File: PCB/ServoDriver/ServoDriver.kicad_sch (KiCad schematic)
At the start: 4 parts, among them Q1 IRF6775M, Q2 IRF6775M, Q3 IRF6775M, Q4 IRF6775M

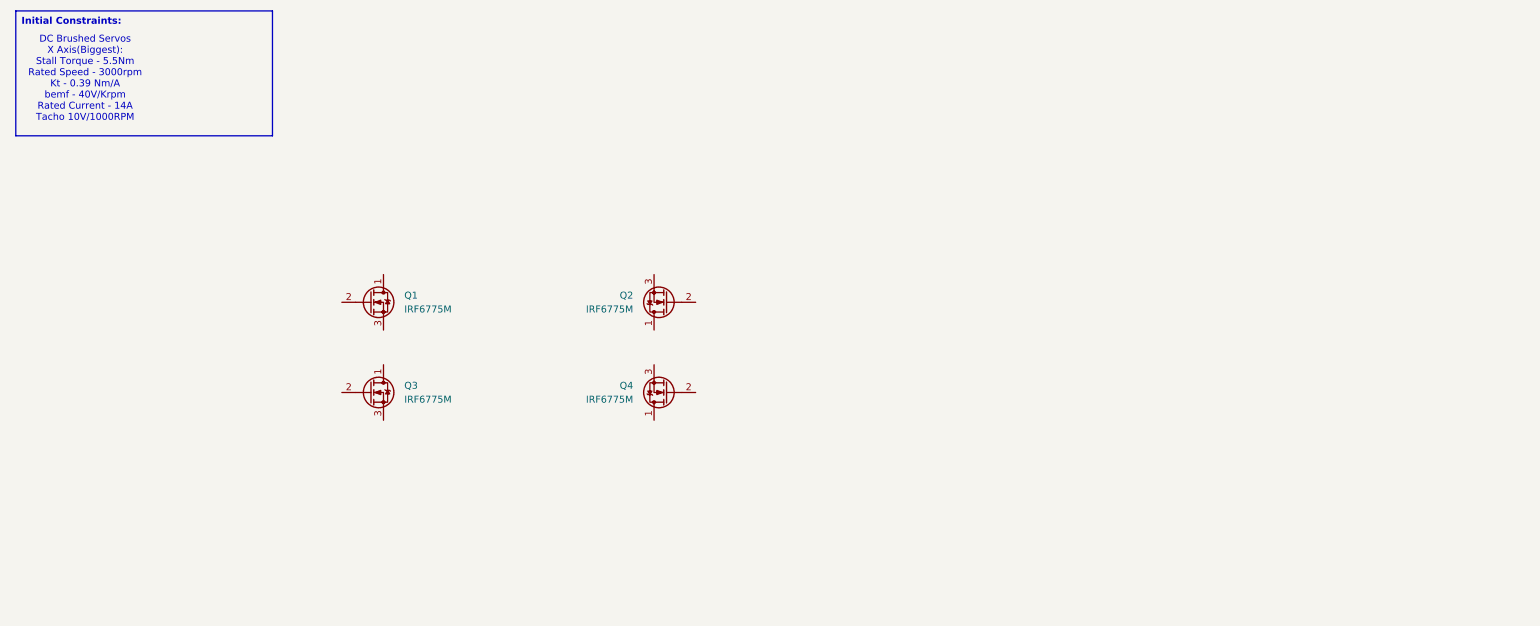
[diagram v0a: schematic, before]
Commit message: H-Bridge & Component Selection
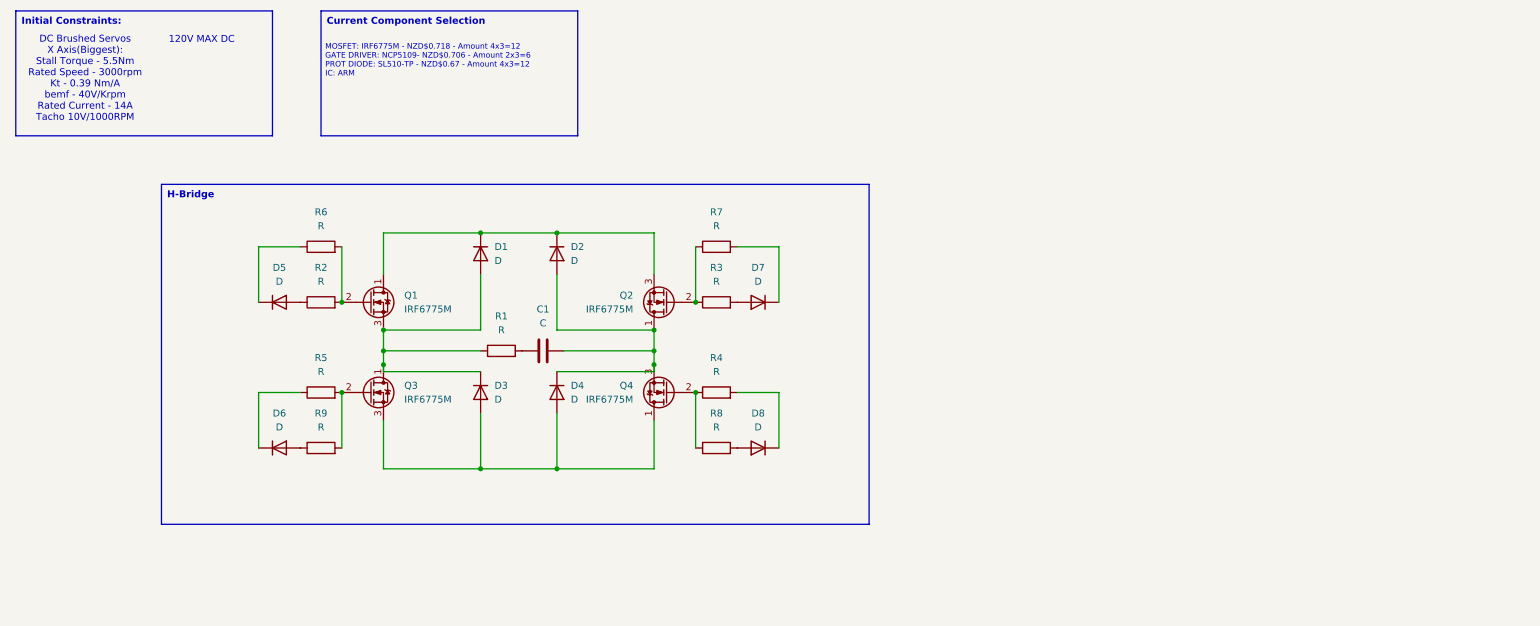
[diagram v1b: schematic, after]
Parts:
- added C1: C, symbol Device:C
- added D1, D2, D3, D4, D5, D6, D7, D8: D, symbol Device:D
- added R1, R2, R3, R4, R5, R6, R7, R8, R9: R, symbol Device:R
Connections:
- net at Q1.1 (D): now also Q2.3 (S), D1.1 (K), D2.1 (K)
- net at Q1.2 (G): now also R2.2, R6.2
- net at Q1.3 (S): now also Q3.1 (D), D1.2 (A), D3.1 (K), R1.1
- net at Q4.1 (D): now also Q3.3 (S), D3.2 (A), D4.2 (A)
- net at Q4.2 (G): now also R4.1, R8.1
- net at Q4.3 (S): now also Q2.1 (D), C1.2, D2.2 (A), D4.1 (K)
- net at Q2.2 (G): now also R3.1, R7.1
- net at Q3.2 (G): now also R5.2, R9.2
- new net: D5.1 (K), R6.1
- new net: D5.2 (A), R2.1
- new net: D8.1 (K), R4.2
- new net: D8.2 (A), R8.2
- new net: D7.2 (A), R3.2
- new net: D6.1 (K), R5.1
- new net: D6.2 (A), R9.1
- new net: D7.1 (K), R7.2
- new net: C1.1, R1.2
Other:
- note added: "120V MAX DC"
- note added: "MOSFET: IRF6775M - NZD$0.718 - Amount 4x3=12 GATE DRIVER: NCP5109- NZD$0.706 - Amount 2x3=6 PROT DIODE: SL510-TP - NZD$0.67 - Amount 4x3=12 IC: ARM"

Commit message: Fusion 360 Archive file
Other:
- note added: "MOSFET: IRF6775M - NZD$0.718 - Amount 4x3=12 GATE DRIVER: NCP5109- NZD$0.706 - Amount 2x3=6 PROT DIODE: SL510-TP - NZD$0.67 - Amount 4x3=12 IC: STM32F031x4"
- note removed: "MOSFET: IRF6775M - NZD$0.718 - Amount 4x3=12 GATE DRIVER: NCP5109- NZD$0.706 - Amount 2x3=6 PROT DIODE: SL510-TP - NZD$0.67 - Amount 4x3=12 IC: ARM"
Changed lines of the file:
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@@
 		)
 	)
-	(text "MOSFET: IRF6775M - NZD$0.718 - Amount 4x3=12\nGATE DRIVER: NCP5109- NZD$0.706 - Amount 2x3=6\nPROT DIODE: SL510-TP - NZD$0.67 - Amount 4x3=12\nIC: ARM\n"
+	(text "MOSFET: IRF6775M - NZD$0.718 - Amount 4x3=12\nGATE DRIVER: NCP5109- NZD$0.706 - Amount 2x3=6\nPROT DIODE: SL510-TP - NZD$0.67 - Amount 4x3=12\nIC: STM32F031x4\n"
 		(exclude_from_sim no)
 		(at 71.882 24.384 0)

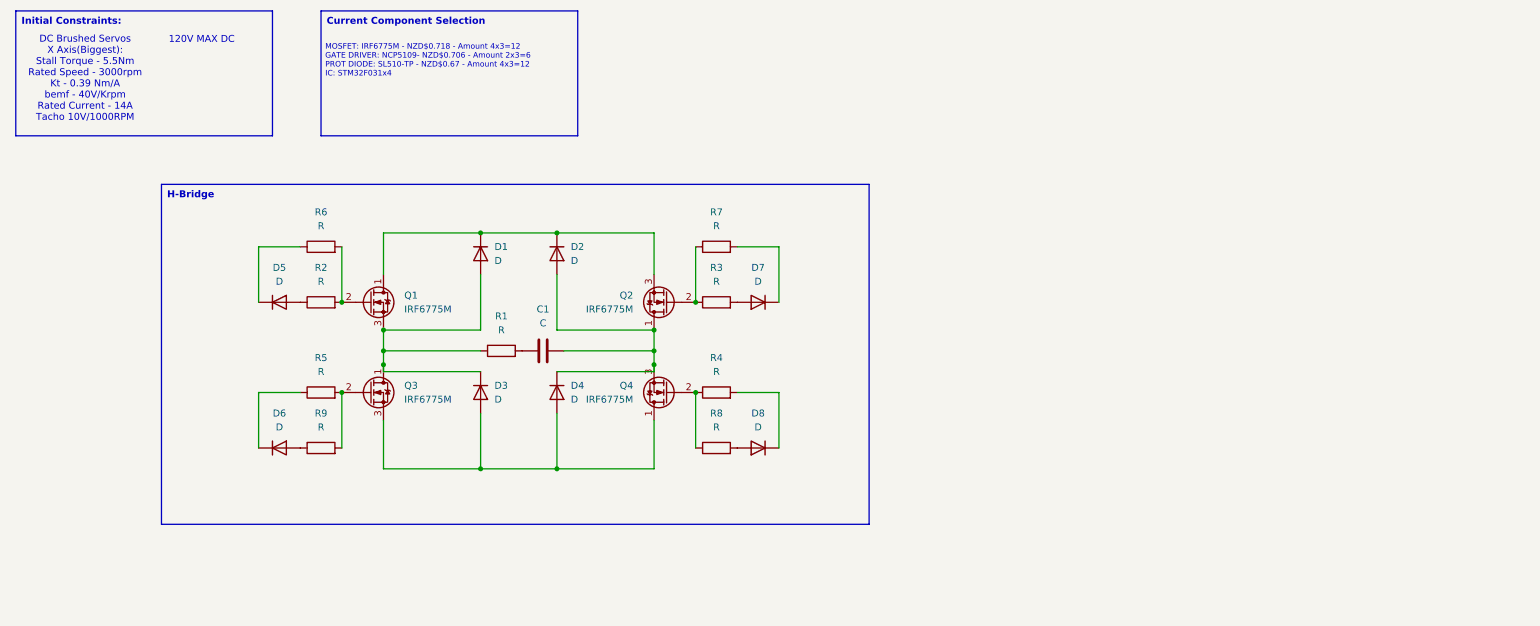
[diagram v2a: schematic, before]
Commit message: Updated Gantry and Frame + Starting Control Algo
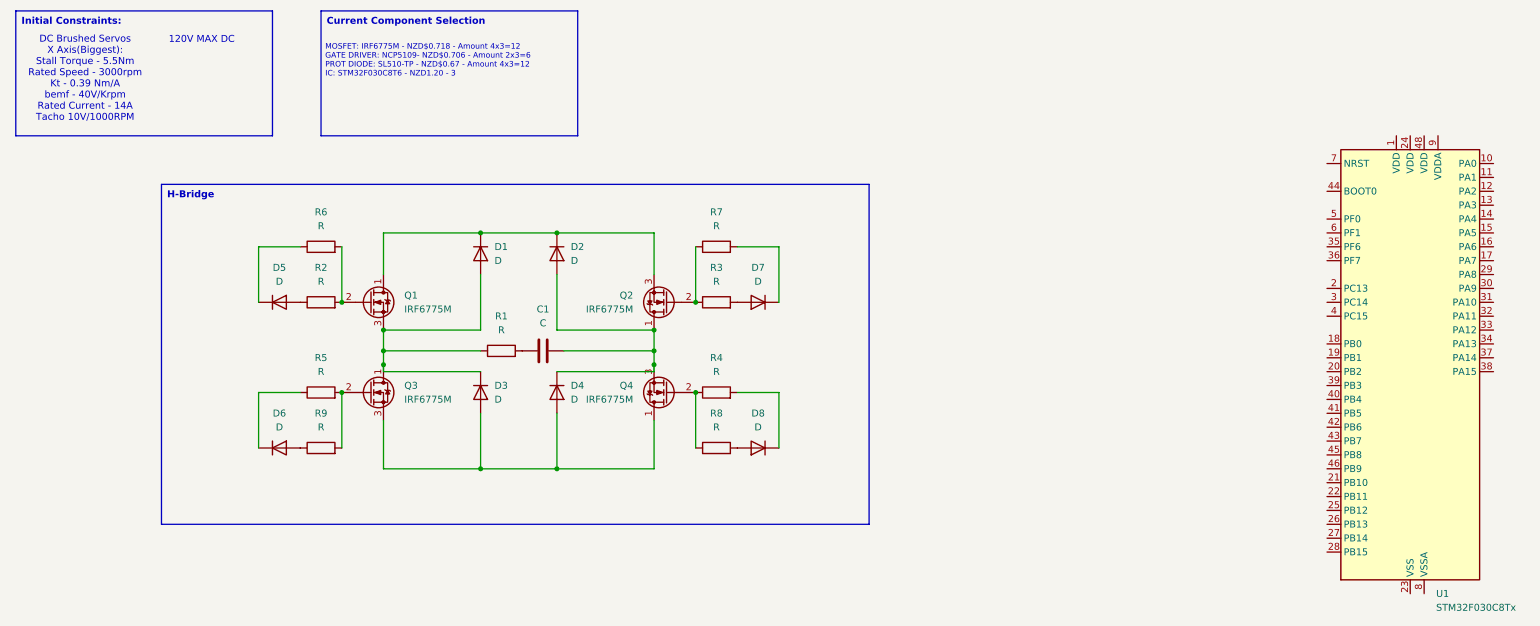
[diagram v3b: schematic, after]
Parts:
- added U1: STM32F030C8Tx, Package_QFP:LQFP-48_7x7mm_P0.5mm, symbol MCU_ST_STM32F0:STM32F030C8Tx
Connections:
- new net: U1.23 (VSS), U1.47 (VSS)
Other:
- note added: "MOSFET: IRF6775M - NZD$0.718 - Amount 4x3=12 GATE DRIVER: NCP5109- NZD$0.706 - Amount 2x3=6 PROT DIODE: SL510-TP - NZD$0.67 - Amount 4x3=12 IC: STM32F030C8T6 - NZD1.20 - 3"
- note removed: "MOSFET: IRF6775M - NZD$0.718 - Amount 4x3=12 GATE DRIVER: NCP5109- NZD$0.706 - Amount 2x3=6 PROT DIODE: SL510-TP - NZD$0.67 - Amount 4x3=12 IC: STM32F031x4"
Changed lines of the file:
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@@
 	(generator "eeschema")
 	(generator_version "8.0")
-	(paper "A4")
+	(paper "A3")
 	(junction
 		(at 100.33 99.06)
@@
 		)
 	)
-	(text "MOSFET: IRF6775M - NZD$0.718 - Amount 4x3=12\nGATE DRIVER: NCP5109- NZD$0.706 - Amount 2x3=6\nPROT DIODE: SL510-TP - NZD$0.67 - Amount 4x3=12\nIC: STM32F031x4\n"
+	(text "MOSFET: IRF6775M - NZD$0.718 - Amount 4x3=12\nGATE DRIVER: NCP5109- NZD$0.706 - Amount 2x3=6\nPROT DIODE: SL510-TP - NZD$0.67 - Amount 4x3=12\nIC: STM32F030C8T6 - NZD1.20 - 3\n"
 		(exclude_from_sim no)
 		(at 71.882 24.384 0)
@@
 					(unit 1)
 				)
+			)
+		)
+	)
+	(symbol
+		(lib_id "MCU_ST_STM32F0:STM32F030C8Tx")
+		(at 270.51 81.28 0)
+		(unit 1)
+		(exclude_from_sim no)
+		(in_bom yes)
+		(on_board yes)
+		(dnp no)
+		(fields_autoplaced yes)
+		(property "Reference" "U1"
+			(at 275.2441 121.92 0)
+			(effects
+				(font
+					(size 1.27 1.27)
+				)
+				(justify left)
+			)
+		)
+		(property "Value" "STM32F030C8Tx"
+			(at 275.2441 124.46 0)
+			(effects
+				(font
+					(size 1.27 1.27)
+				)
+				(justify left)
+			)
+		)
+		(property "Footprint" "Package_QFP:LQFP-48_7x7mm_P0.5mm"
+			(at 257.81 119.38 0)
+			(effects
+				(font
+					(size 1.27 1.27)
+				)
+				(justify right)
+				(hide yes)
+			)
+		)
+		(property "Datasheet" "https://www.st.com/resource/en/datasheet/stm32f030c8.pdf"
+			(at 270.51 81.28 0)
+			(effects
+				(font
+					(size 1.27 1.27)
+				)
+				(hide yes)
+			)
+		)
+		(property "Description" "STMicroelectronics Arm Cortex-M0 MCU, 64KB flash, 8KB RAM, 48 MHz, 2.4-3.6V, 39 GPIO, LQFP48"
+			(at 270.51 81.28 0)
+			(effects
+				(font
+					(size 1.27 1.27)
+				)
+				(hide yes)
+			)
+		)
+		(pin "1"
+		)
+		(pin "20"
+		)
+		(pin "12"
+		)
+		(pin "18"
+		)
+		(pin "10"
+		)
+		(pin "15"
+		)
+		(pin "13"
+		)
+		(pin "2"
+		)
+		(pin "41"
+		)
+		(pin "46"
+		)
+		(pin "30"
+		)
+		(pin "4"
+		)
+		(pin "48"
+		)
+		(pin "9"
+		)
+		(pin "31"
+		)
+		(pin "25"
+		)
+		(pin "22"
+		)
+		(pin "37"
+		)
+		(pin "26"
+		)
+		(pin "17"
+		)
+		(pin "19"
+		)
+		(pin "5"
+		)
+		(pin "40"
+		)
+		(pin "28"
+		)
+		(pin "35"
+		)
+		(pin "42"
+		)
+		(pin "21"
+		)
+		(pin "47"
+		)
+		(pin "29"
+		)
+		(pin "32"
+		)
+		(pin "23"
+		)
+		(pin "34"
+		)
+		(pin "44"
+		)
+		(pin "45"
+		)
+		(pin "33"
+		)
+		(pin "16"
+		)
+		(pin "36"
+		)
+		(pin "11"
+		)
+		(pin "14"
+		)
+		(pin "27"
+		)
+		(pin "38"
+		)
+		(pin "3"
+		)
+		(pin "39"
+		)
+		(pin "24"
+		)
+		(pin "43"
+		)
+		(pin "6"
+		)
+		(pin "7"
+		)
+		(pin "8"
+		)
+		(instances
+			(project ""
+				(path "/03dc4c26-7d66-48c6-976c-6bbf186a5b7f"
+					(reference "U1")
+					(unit 1)
+				)
